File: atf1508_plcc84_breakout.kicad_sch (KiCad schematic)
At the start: 13 parts, among them J1 Atmel-JTAG-10, J2 Conn_01x34, J3 Conn_01x34, U1 ATF1508AS-xJx84

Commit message: Update
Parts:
- J2, J3: value Conn_01x34 -> Conn_01x35
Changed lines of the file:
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@@
       (effects (font (size 1.27 1.27)) (justify left))
     )
-    (property "Value" "Conn_01x34" (id 1) (at 219.71 88.8999 0)
+    (property "Value" "Conn_01x35" (id 1) (at 219.71 88.8999 0)
       (effects (font (size 1.27 1.27)) (justify left))
     )
@@
   (symbol (lib_id "Connector_Generic:Conn_01x35") (at 254 86.36 0) (unit 1)
     (in_bom yes) (on_board yes) (fields_autoplaced)
-    (property "Reference" "J3" (id 0) (at 256.54 86.3599 0)
-      (effects (font (size 1.27 1.27)) (justify left))
-    )
-    (property "Value" "Conn_01x34" (id 1) (at 256.54 88.8999 0)
+    (property "Reference" "J3" (id 0) (at 256.54 85.0899 0)
+      (effects (font (size 1.27 1.27)) (justify left))
+    )
+    (property "Value" "Conn_01x35" (id 1) (at 256.54 87.6299 0)
       (effects (font (size 1.27 1.27)) (justify left))
     )
@@
     )
     (path "/988630f3-be3d-4fb3-beb3-3ce4d5f04e12"
-      (reference "J2") (unit 1) (value "Conn_01x34") (footprint "Connector_PinHeader_2.54mm:PinHeader_1x35_P2.54mm_Vertical")
+      (reference "J2") (unit 1) (value "Conn_01x35") (footprint "Connector_PinHeader_2.54mm:PinHeader_1x35_P2.54mm_Vertical")
     )
     (path "/eca2a06c-4bef-48fd-bdd8-b79f382b48a4"
-      (reference "J3") (unit 1) (value "Conn_01x34") (footprint "Connector_PinHeader_2.54mm:PinHeader_1x35_P2.54mm_Vertical")
+      (reference "J3") (unit 1) (value "Conn_01x35") (footprint "Connector_PinHeader_2.54mm:PinHeader_1x35_P2.54mm_Vertical")
     )
     (path "/dfb01301-6794-49fe-8f84-ac59cd5daae2"

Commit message: Update
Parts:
- removed C1: 10u, Capacitor_SMD:C_0805_2012Metric_Pad1.18x1.45mm_HandSolder, symbol Device:C_Small
- added C1: 10u, Capacitor_THT:CP_Radial_D4.0mm_P1.50mm, symbol Device:C_Polarized_Small
- added C10: 100n, Capacitor_SMD:C_0805_2012Metric_Pad1.18x1.45mm_HandSolder, symbol Device:C_Small
- added X1: xMHz, Oscillator:Oscillator_SMD_IQD_IQXO70-4Pin_7.5x5.0mm_HandSoldering, symbol Oscillator:CFPS-72
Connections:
- net GND: now also C1.2, C10.1, X1.2 (GND)
- net I/GCLK1: now also X1.3 (Output)
- net VCC: now also C1.1, C10.2, X1.1 (EN), X1.4 (+Vs)
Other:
- note added: "Optional footprint for SMD clock oscillator connected to GCLK1"
- moved on the sheet: J1

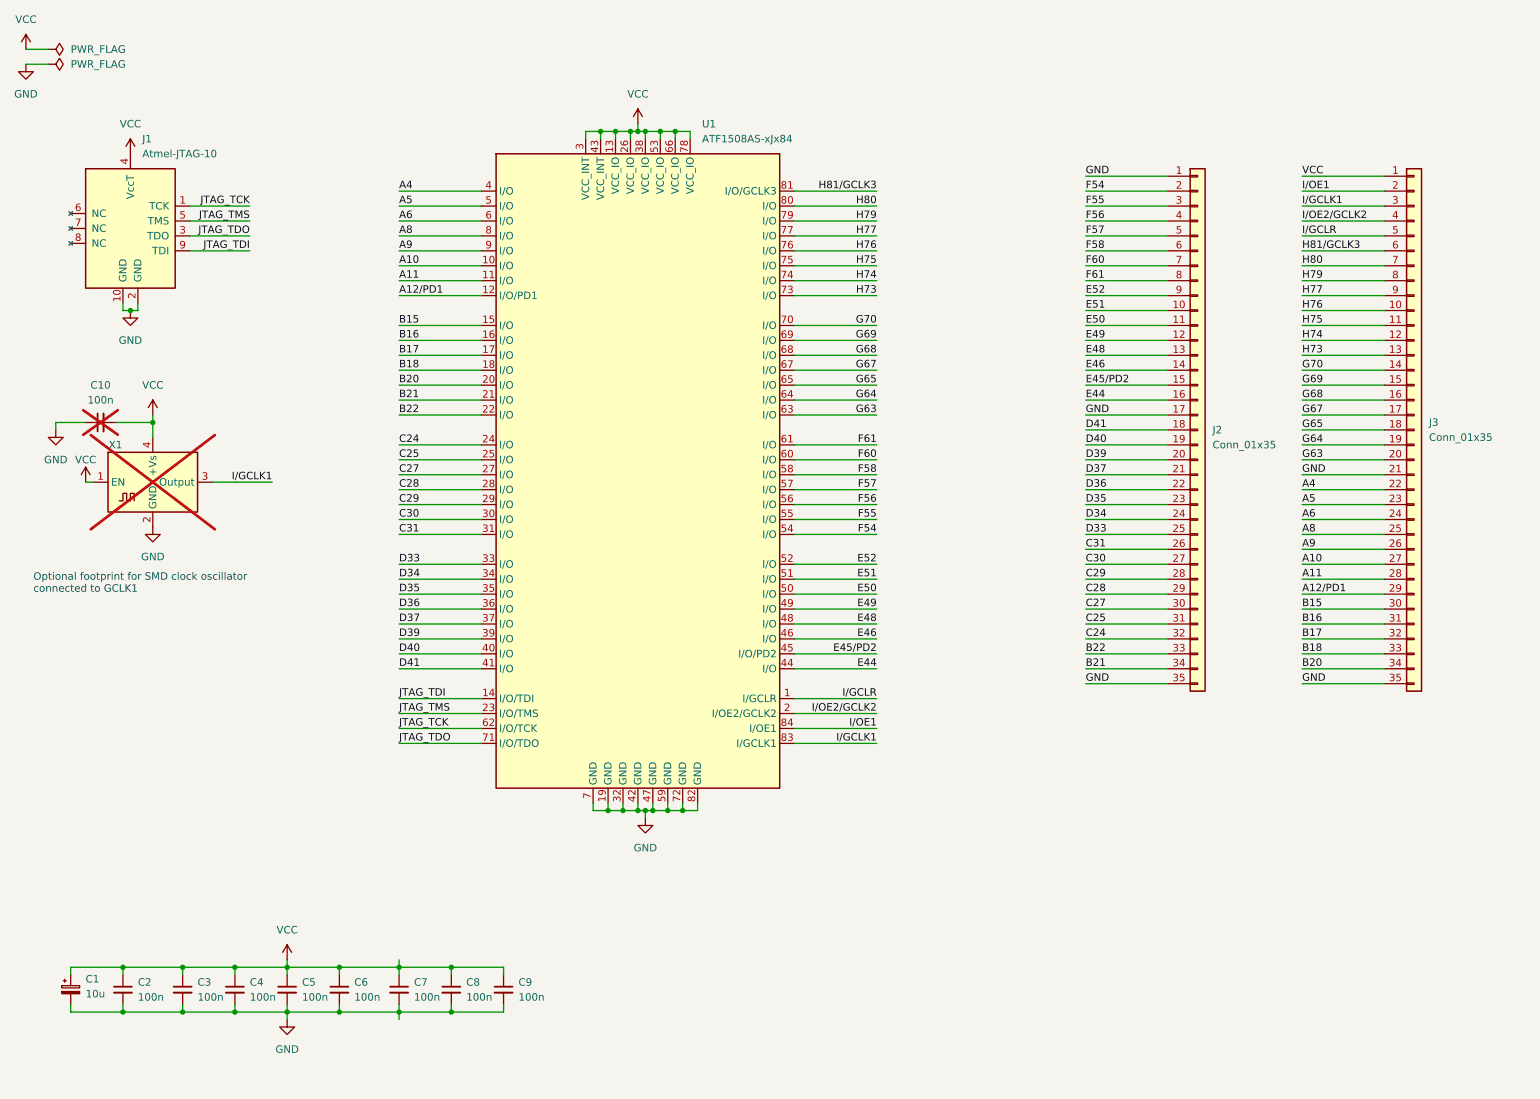
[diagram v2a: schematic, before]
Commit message: Revert oscillator addition
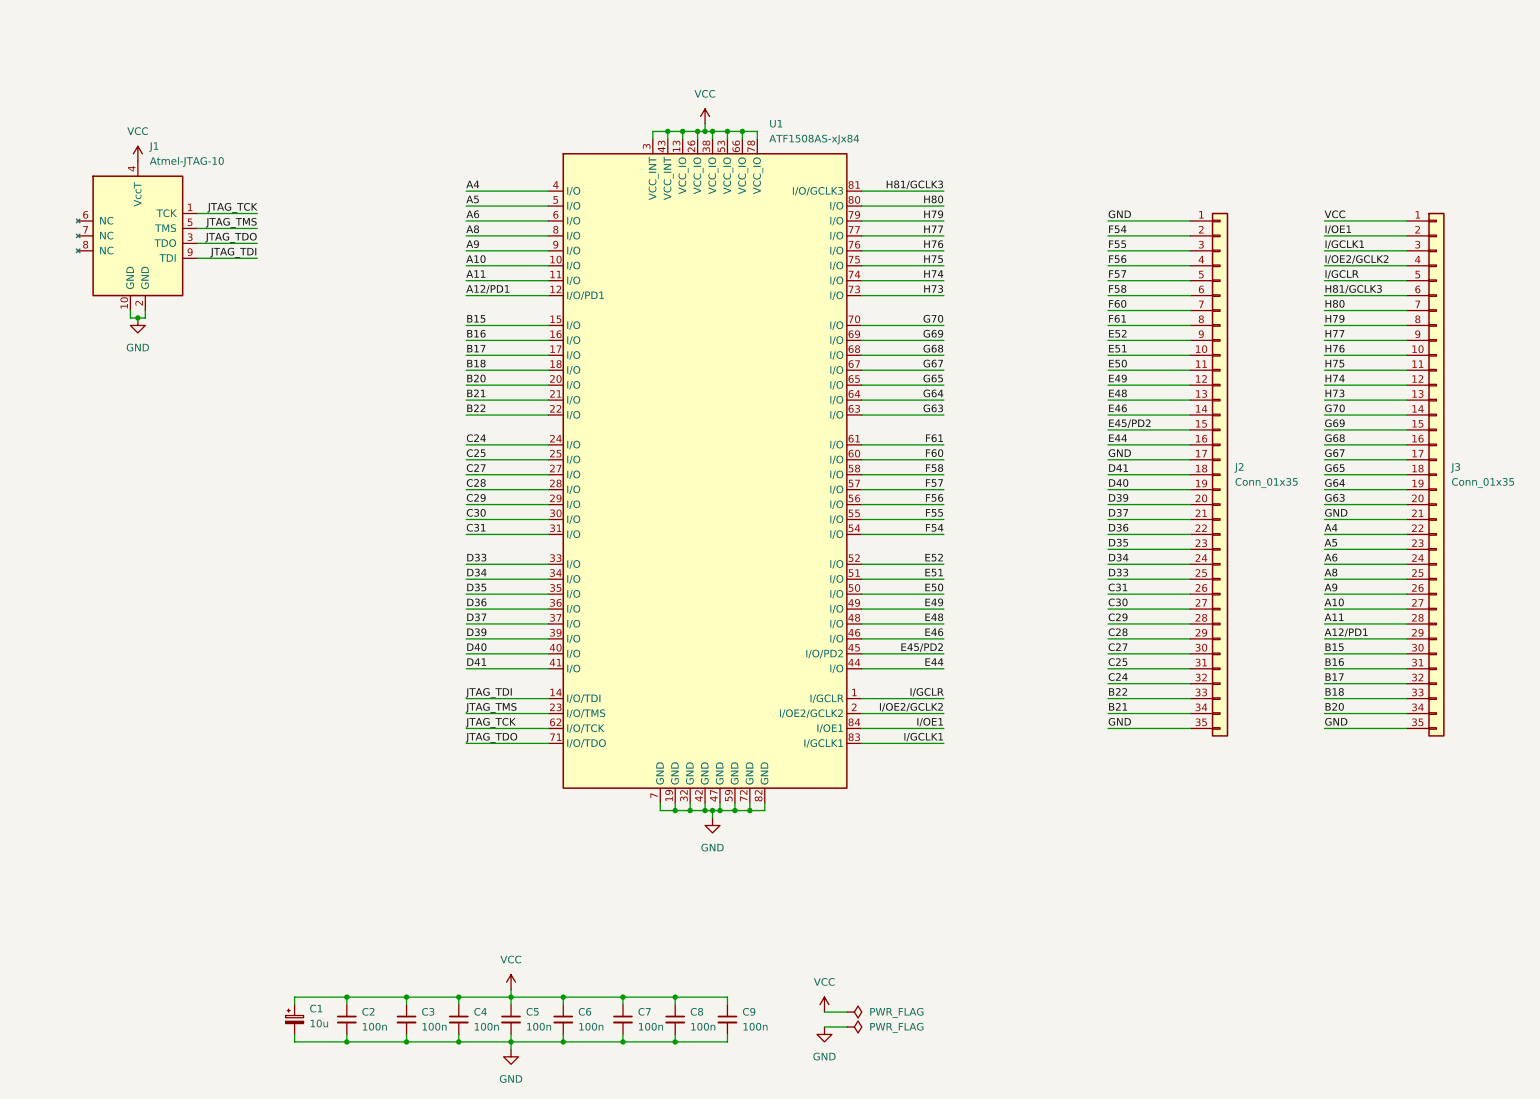
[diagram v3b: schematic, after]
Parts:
- removed C10: 100n, Capacitor_SMD:C_0805_2012Metric_Pad1.18x1.45mm_HandSolder, symbol Device:C_Small
- removed X1: xMHz, Oscillator:Oscillator_SMD_IQD_IQXO70-4Pin_7.5x5.0mm_HandSoldering, symbol Oscillator:CFPS-72
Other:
- note removed: "Optional footprint for SMD clock oscillator connected to GCLK1"
- moved on the sheet: C1, C2, C3, C4, C5, C6, C7, C8, C9, J1, U1

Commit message: Add pin numbers for global inputs and re-order them
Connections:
- net I/GCLK1: now also J3.5 (Pin_5); no longer J3.3 (Pin_3)
- net I/GCLR: now also J3.3 (Pin_3); no longer J3.5 (Pin_5)
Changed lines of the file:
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@@
   (title_block
     (title "ATF1508 PLCC84 Breakout")
-    (date "2023-06-17")
-    (rev "A")
+    (date "2023-07-15")
+    (rev "B")
     (comment 2 "https://github.com/adrienkohlbecker/atf1508_plcc84_breakout")
     (comment 3 "Licensed under CERN-OHL-W v2")
@@
     (effects (font (size 1.27 1.27)) (justify left bottom))
   )
-  (label "I{slash}GCLR" (at 238.76 60.96 0) (fields_autoplaced)
+  (label "I{slash}GCLR" (at 238.76 55.88 0) (fields_autoplaced)
     (effects (font (size 1.27 1.27)) (justify left bottom))
   )
@@
     (effects (font (size 1.27 1.27)) (justify left bottom))
   )
-  (label "I{slash}GCLK1" (at 238.76 55.88 0) (fields_autoplaced)
-    (effects (font (size 1.27 1.27)) (justify left bottom))
-  )
+  (label "I{slash}GCLK1" (at 238.76 60.96 0) (fields_autoplaced)
+    (effects (font (size 1.27 1.27)) (justify left bottom))
+  )
